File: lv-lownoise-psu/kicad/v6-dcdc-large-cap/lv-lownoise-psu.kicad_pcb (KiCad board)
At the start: 2 copper layers, 91.5 x 76.8 mm, 67 parts, among them J1 AC, J10 GND, J11 -25V, J13 EARTH, J15 +25V, J2 GND, J3 AC, J4 +15V, J5 GND, J6 -15V, J7 LED, J8 GND, J9 +5V, Q1 BD139, Q2 BD140, U1 AP63205WU, U3 LT3045xMSE, U4 LT3094xMSE

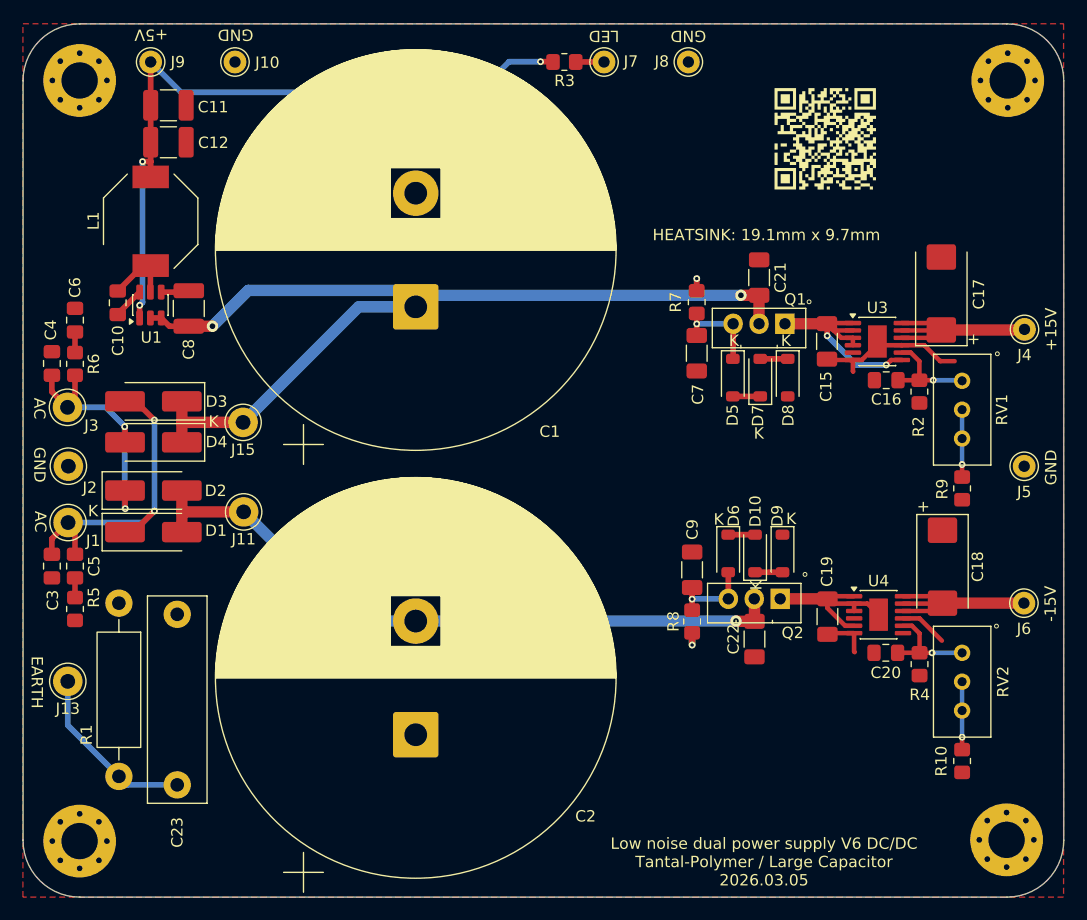
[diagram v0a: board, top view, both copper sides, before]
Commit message: Update with new inductor for buck converter
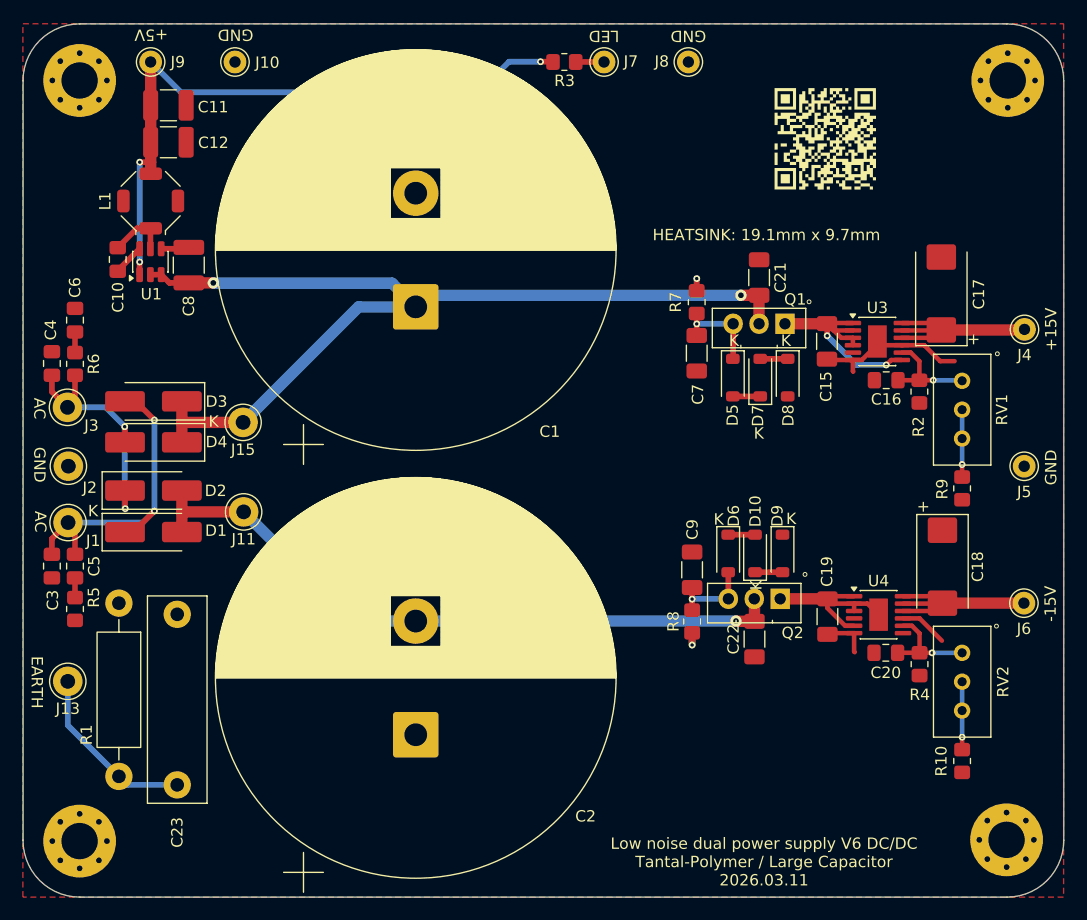
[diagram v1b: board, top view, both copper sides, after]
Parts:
- C8: value 10uF/100V/X7R -> 10uF/50V/X7R
- L1: footprint Inductor_SMD:L_Bourns-SRU8028_8.0x8.0mm -> Inductor_SMD:L_Bourns_SRU5016_5.2x5.2mm
- moved C10 3.81 mm to (88.3, 50.0)
- moved C8 3.81 mm to (94.6, 50.5)
- moved U1 3.81 mm to (91.2, 50.2)
- moved L1 1.78 mm to (91.2, 44.9)
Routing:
- net /VOUT: track 62.3 -> 58.3 mm
- net Net-(D3-K): track 89.6 -> 88.6 mm
- net /SWOUT: track 6.16 -> 5.41 mm
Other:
- board text added: "Low noise dual power supply V6 DC/DC Tantal-Polymer / Large Capacitor 2026.03.11"
- board text removed: "Low noise dual power supply V6 DC/DC Tantal-Polymer / Large Capacitor 2026.03.05"
